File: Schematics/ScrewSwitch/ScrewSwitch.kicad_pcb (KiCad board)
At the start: 2 copper layers, 8.1 x 20.3 mm, 4 parts, among them J1 Mount, J2 BottomPad, J3 TopPad, J4 Mount

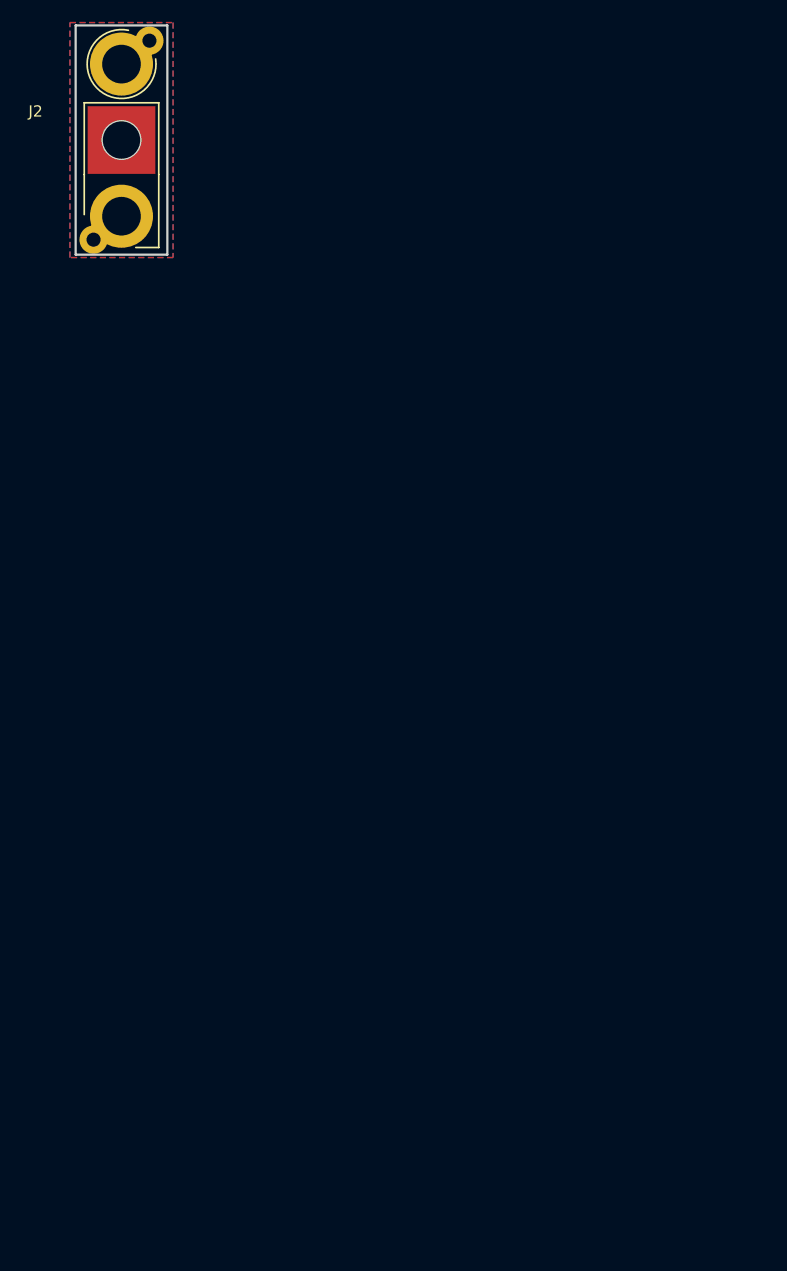
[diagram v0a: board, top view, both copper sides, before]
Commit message: Finished draft of screw switch PCB
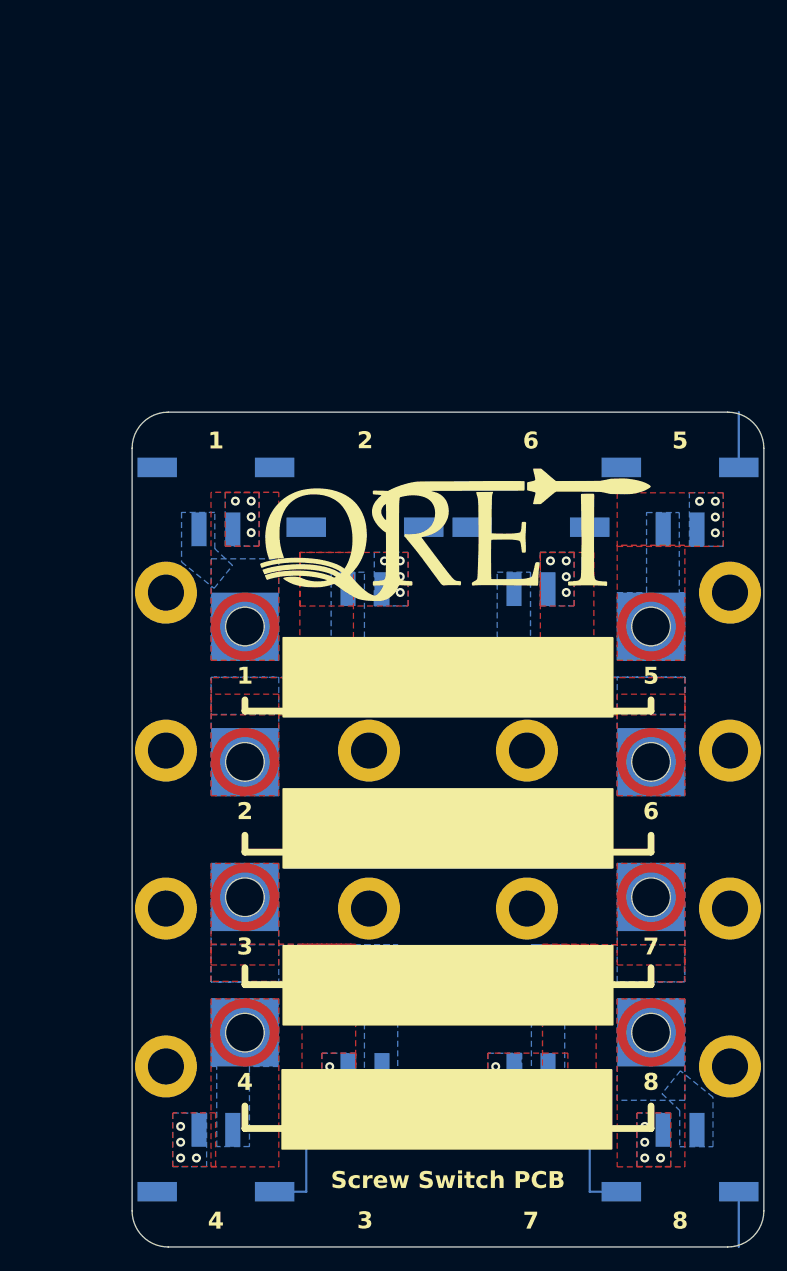
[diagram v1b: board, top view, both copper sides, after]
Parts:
- added H1: MountingHole, MountingHole:MountingHole_3.2mm_M3_ISO14580_Pad, F.Cu at (103.0, 96.0)
- added H10: MountingHole, MountingHole:MountingHole_3.2mm_M3_ISO14580_Pad, F.Cu at (135.0, 124.0)
- added H11: MountingHole, MountingHole:MountingHole_3.2mm_M3_ISO14580_Pad, F.Cu at (153.0, 110.0)
- added H12: MountingHole, MountingHole:MountingHole_3.2mm_M3_ISO14580_Pad, F.Cu at (153.0, 124.0)
- added H2: MountingHole, MountingHole:MountingHole_3.2mm_M3_ISO14580_Pad, F.Cu at (153.0, 138.0)
- added H3: MountingHole, MountingHole:MountingHole_3.2mm_M3_ISO14580_Pad, F.Cu at (121.0, 110.0)
- added H4: MountingHole, MountingHole:MountingHole_3.2mm_M3_ISO14580_Pad, F.Cu at (103.0, 138.0)
- added H5: MountingHole, MountingHole:MountingHole_3.2mm_M3_ISO14580_Pad, F.Cu at (121.0, 124.0)
- added H6: MountingHole, MountingHole:MountingHole_3.2mm_M3_ISO14580_Pad, F.Cu at (153.0, 96.0)
- added H7: MountingHole, MountingHole:MountingHole_3.2mm_M3_ISO14580_Pad, F.Cu at (103.0, 124.0)
- added H8: MountingHole, MountingHole:MountingHole_3.2mm_M3_ISO14580_Pad, F.Cu at (103.0, 110.0)
- added H9: MountingHole, MountingHole:MountingHole_3.2mm_M3_ISO14580_Pad, F.Cu at (135.0, 110.0)
- added J5: CH4, footprints:CONN_2-1445057-2_TYCO, B.Cu at (105.9, 143.6)
- added J6: CH3, footprints:CONN_2-1445057-2_TYCO, B.Cu at (119.1, 138.3)
- added J7: CH7, footprints:CONN_2-1445057-2_TYCO, B.Cu at (133.9, 138.3)
- added J8: CH8, footprints:CONN_2-1445057-2_TYCO, B.Cu at (147.1, 143.6)
- added SW1: ~, ScrewSwitchLibrary:ScrewSwitchNew, F.Cu at (110.0, 99.0)
- added SW2: ~, ScrewSwitchLibrary:ScrewSwitchNew, F.Cu at (110.0, 111.0)
- added SW3: ~, ScrewSwitchLibrary:ScrewSwitchNew, F.Cu at (110.0, 123.0)
- added SW4: ~, ScrewSwitchLibrary:ScrewSwitchNew, F.Cu at (110.0, 135.0)
- added SW5: ~, ScrewSwitchLibrary:ScrewSwitchNew, F.Cu at (146.0, 99.0)
- added SW6: ~, ScrewSwitchLibrary:ScrewSwitchNew, F.Cu at (146.0, 111.0)
- added SW7: ~, ScrewSwitchLibrary:ScrewSwitchNew, F.Cu at (146.0, 123.0)
- added SW8: ~, ScrewSwitchLibrary:ScrewSwitchNew, F.Cu at (146.0, 135.0)
- J1: value Mount -> CH5; footprint ScrewSwitchLibrary:ScrewTermMount -> footprints:CONN_2-1445057-2_TYCO; moved to B.Cu
- J2: value BottomPad -> CH6; footprint ScrewSwitchLibrary:ScrewTermBack -> footprints:CONN_2-1445057-2_TYCO; moved to B.Cu
- J3: value TopPad -> CH2; footprint ScrewSwitchLibrary:ScrewTermFront -> footprints:CONN_2-1445057-2_TYCO; moved to B.Cu
- J4: value Mount -> CH1; footprint ScrewSwitchLibrary:ScrewTermMount -> footprints:CONN_2-1445057-2_TYCO; moved to B.Cu
- moved J1 65.6 mm to (150.1, 90.4), turned to 180 degrees
- moved J2 54.9 mm to (136.9, 95.7), turned to 180 degrees
- moved J3 46.0 mm to (122.1, 95.7), turned to 180 degrees
- moved J4 29.5 mm to (108.9, 90.4), turned to 180 degrees
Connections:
- J1 pad 1: /bot -> /Top5
- J2 pad 1: /top -> /Top6
- J4 pad 1: /top -> /Top1
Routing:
- net /Top8: vias 0 -> 4
- net /Top7: vias 0 -> 4
- net /Top6: vias 0 -> 4
- net /Top5: vias 0 -> 4
- net /Top4: vias 0 -> 4
- net /Top3: vias 0 -> 4
- net /Top2: vias 0 -> 4
- net /Top1: vias 0 -> 4
- added copper zone on B.Cu, net /Bot1
- added copper zone on B.Cu, net /Bot2
- added copper zone on B.Cu, net /Bot3
- added copper zone on B.Cu, net /Bot4
- added copper zone on B.Cu, net /Bot5
- added copper zone on B.Cu, net /Bot6
- added copper zone on B.Cu, net /Bot7
- added copper zone on B.Cu, net /Bot8
- added copper zone on B.Cu, net /Top1
- added copper zone on F.Cu, net /Top1
- added copper zone on B.Cu, net /Top2
- added copper zone on F.Cu, net /Top2
- added copper zone on B.Cu, net /Top3
- added copper zone on F.Cu, net /Top3
- added copper zone on B.Cu, net /Top4
- added copper zone on F.Cu, net /Top4
- added copper zone on B.Cu, net /Top5
- added copper zone on F.Cu, net /Top5
- added copper zone on B.Cu, net /Top6
- added copper zone on F.Cu, net /Top6
- added copper zone on B.Cu, net /Top7
- added copper zone on F.Cu, net /Top7
- added copper zone on B.Cu, net /Top8
- added copper zone on F.Cu, net /Top8
- removed copper zone on B.Cu, net /bot
- removed copper zone on F.Cu, net /top
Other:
- board size 8.1 x 20.3 mm -> 56 x 74 mm
- board text added: "1"
- board text added: "2"
- board text added: "3"
- board text added: "4"
- board text added: "5"
- board text added: "6"
- board text added: "7"
- board text added: "8"
- board text added: "?????? Rev 1.0 QRET Mar 2025 Kennan Bays Owen Price"
- board text added: "Screw Switch PCB"

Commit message: Final prep for fab
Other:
- board text added: "NECTAR Rev 1.0 QRET Mar 2025 Kennan Bays Owen Price"
- board text added: "NECTAR Screw Switch PCB"
- board text removed: "?????? Rev 1.0 QRET Mar 2025 Kennan Bays Owen Price"
- board text removed: "Screw Switch PCB"
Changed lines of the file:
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@@
     (effects (font (size 1.5 1.5) (thickness 0.25) bold) (justify top mirror))
   )
-  (gr_text "?????? Rev 1.0\nQRET Mar 2025\n\n\n\nKennan Bays\nOwen Price" (at 128 102.5) (layer "B.SilkS")
+  (gr_text "NECTAR Rev 1.0\nQRET Mar 2025\n\n\n\nKennan Bays\nOwen Price" (at 128 102.5) (layer "B.SilkS")
     (effects (font (size 1.5 1.5) (thickness 0.25)) (justify top mirror))
   )
@@
     (effects (font (size 1.5 1.5) (thickness 0.25) bold) (justify top))
   )
-  (gr_text "Screw Switch PCB" (at 128 147.2) (layer "F.SilkS" knockout)
+  (gr_text "NECTAR Screw Switch PCB" (at 128 147.2) (layer "F.SilkS" knockout)
     (effects (font (size 1.5 1.5) (thickness 0.25) bold) (justify top))
   )

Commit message: Silkscreen adjustment
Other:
- board text added: "Kennan Bays Owen Price ScrewSwitch PCB Rev 1.0 QRET Mar 2025"
- board text removed: "NECTAR Rev 1.0 QRET Mar 2025 Kennan Bays Owen Price"
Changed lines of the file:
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@@
       (drillshape 0)
       (scaleselection 1)
-      (outputdirectory "ScrewSwitch-Gerbers")
+      (outputdirectory "gerbers/")
     )
   )
@@
     (effects (font (size 1.5 1.5) (thickness 0.25) bold) (justify top mirror))
   )
-  (gr_text "NECTAR Rev 1.0\nQRET Mar 2025\n\n\n\nKennan Bays\nOwen Price" (at 128 102.5) (layer "B.SilkS")
+  (gr_text "Kennan Bays\nOwen Price\n\n\n\nScrewSwitch PCB\nRev 1.0\nQRET Mar 2025" (at 128 101.7) (layer "B.SilkS")
     (effects (font (size 1.5 1.5) (thickness 0.25)) (justify top mirror))
   )
